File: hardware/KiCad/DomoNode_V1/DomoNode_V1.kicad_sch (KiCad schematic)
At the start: 9 parts, among them Q1 Q_NPN, SW1 SW_Push, U1 PIC16F1939

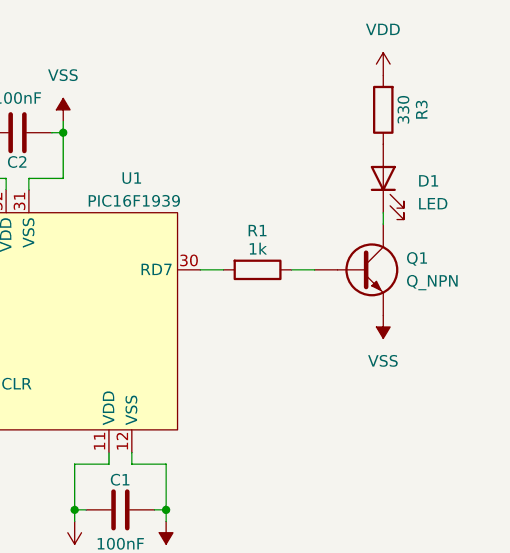
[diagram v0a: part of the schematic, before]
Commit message: docs: actualizar esquema de KiCad con numeración de pines y documentación de hardware
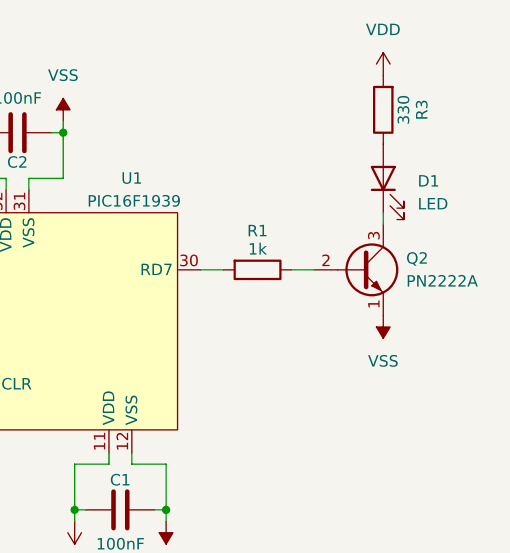
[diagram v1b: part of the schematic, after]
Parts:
- removed Q1: Q_NPN, symbol Device:Q_NPN
- added Q2: PN2222A, Package_TO_SOT_THT:TO-92_Inline, symbol Transistor_BJT:PN2222A
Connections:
- net VSS: now also Q2.1 (E)
- net at D1.1 (K): now also Q2.3 (C)
- net at R1.1: now also Q2.2 (B)
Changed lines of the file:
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@@
 	)
 	(symbol
-		(lib_id "Device:Q_NPN")
+		(lib_id "Transistor_BJT:PN2222A")
 		(at 130.81 55.88 0)
 		(unit 1)
@@
 		(dnp no)
 		(fields_autoplaced yes)
-		(property "Reference" "Q1"
+		(property "Reference" "Q2"
 			(at 135.89 54.6099 0)
 			(effects
@@
 			)
 		)
-		(property "Value" "Q_NPN"
+		(property "Value" "PN2222A"
 			(at 135.89 57.1499 0)
 			(effects
@@
 			)
 		)
-		(property "Footprint" ""
-			(at 135.89 53.34 0)
+		(property "Footprint" "Package_TO_SOT_THT:TO-92_Inline"
+			(at 135.89 57.785 0)
+			(effects
+				(font
+					(size 1.27 1.27)
+					(italic yes)
+				)
+				(justify left)
+				(hide yes)
+			)
+		)
+		(property "Datasheet" "https://www.onsemi.com/pub/Collateral/PN2222-D.PDF"
+			(at 130.81 55.88 0)
 			(effects
 				(font
 					(size 1.27 1.27)
 				)
+				(justify left)
 				(hide yes)
 			)
 		)
-		(property "Datasheet" "~"
+		(property "Description" "1A Ic, 40V Vce, NPN Transistor, General Purpose Transistor, TO-92"
 			(at 130.81 55.88 0)
 			(effects
@@
 			)
 		)
-		(property "Description" "NPN bipolar junction transistor"
+		(property "Sim.Device" "NPN"
 			(at 130.81 55.88 0)
 			(effects
@@
 			)
 		)
-		(pin "E"
+		(property "Sim.Pins" "1=E 2=B 3=C"
+			(at 130.81 55.88 0)
+			(effects
+				(font
+					(size 1.27 1.27)
+				)
+				(hide yes)
+			)
 		)
-		(pin "C"
+		(pin "2"
 		)
-		(pin "B"
+		(pin "3"
+		)
+		(pin "1"
 		)
 		(instances
 			(project ""
 				(path "/6364ebdf-2692-4c4c-832e-1a57d48926ff"
-					(reference "Q1")
+					(reference "Q2")
 					(unit 1)
 				)

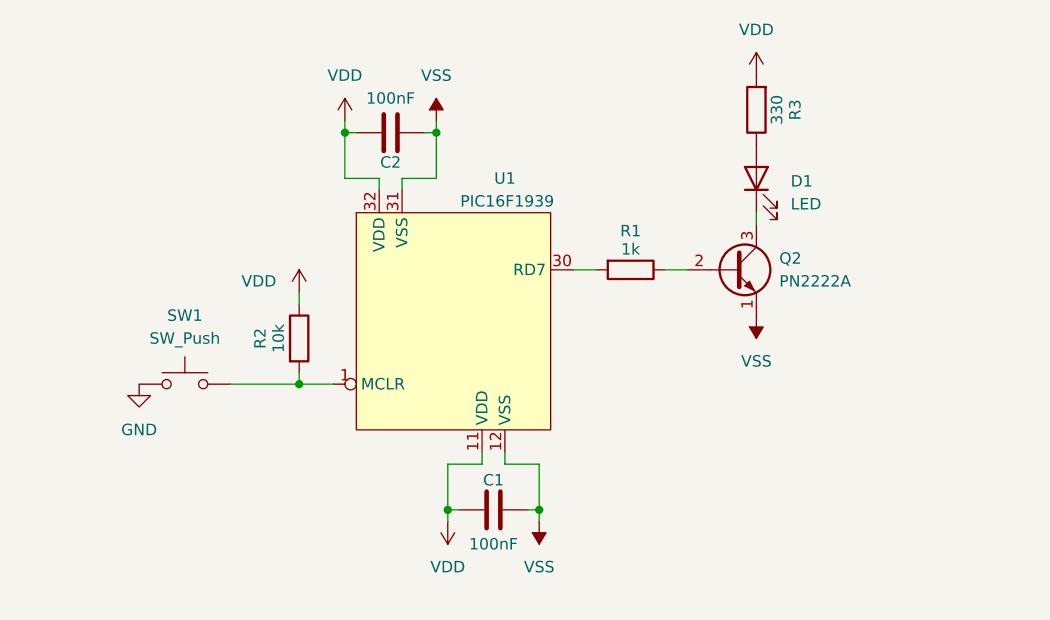
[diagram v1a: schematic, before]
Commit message: hardware: integrar puerto de programación ICSP para PICkit3 en el esquema principal
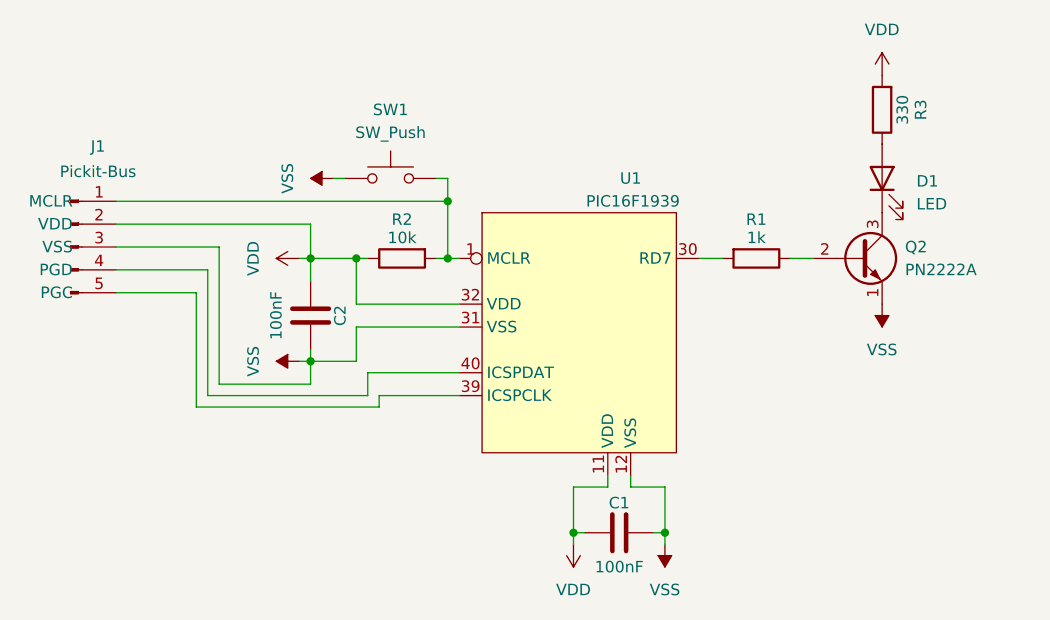
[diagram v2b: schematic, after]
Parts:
- added J1: Pickit-Bus, symbol Connector:Conn_01x05_Pin
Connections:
- net GND is gone; now on net VSS: SW1.1
- net VDD: now also J1.2 (VDD)
- net VSS: now also J1.3 (VSS)
- net at R2.2, SW1.2, U1.1 (MCLR): now also J1.1 (MCLR)
- new net: J1.4 (PGD), U1.40 (ICSPDAT)
- new net: J1.5 (PGC), U1.39 (ICSPCLK)
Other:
- moved on the sheet: C1, C2, D1, Q2, R1, R2, R3, SW1

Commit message: - Actualización de registros del cajetín para la Iteración 02. - Adición de terminales UART (TX/RX) y puerto de conexión USB-TTL. - Configuración de componentes para validación de telemetría a 9600 bps. - Exportación de diagramas técnicos actualizados (PDF e Inkscape).
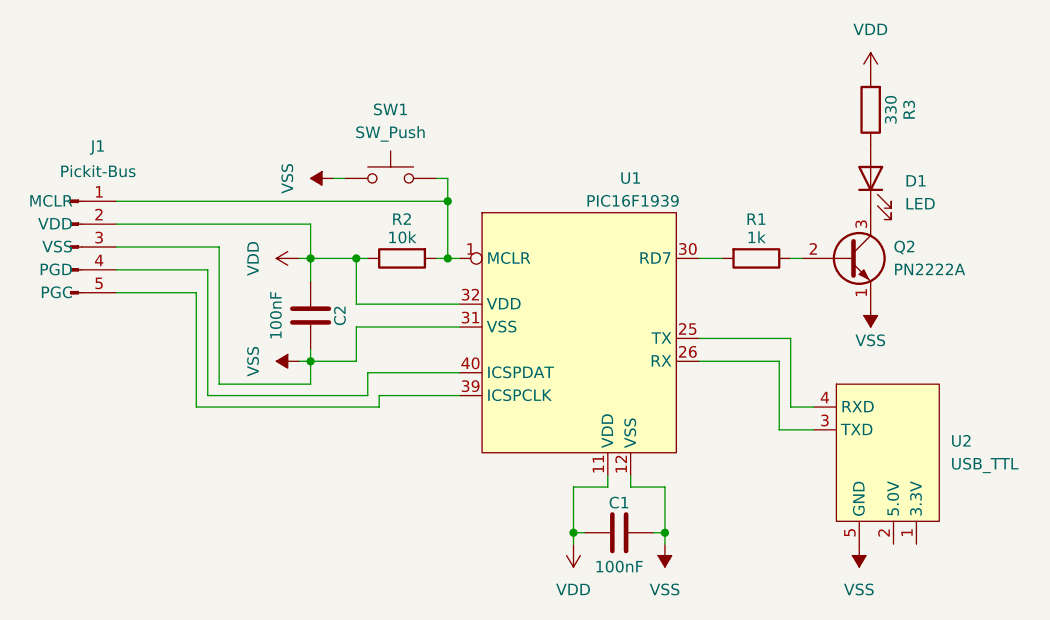
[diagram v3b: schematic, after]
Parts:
- added U2: USB_TTL, symbol DomoNode:USB_TTL
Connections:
- net VSS: now also U2.5 (GND)
- new net: U1.25 (TX), U2.4 (RXD)
- new net: U1.26 (RX), U2.3 (TXD)
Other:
- title: Módulo de Salida LED y Entrada de Control -> DomoNode: Validación de Telemetría UART
- moved on the sheet: D1, Q2, R3
